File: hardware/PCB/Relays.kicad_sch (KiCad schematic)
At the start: 22 parts, among them K601 SANYOU_SRD_Form_C, K602 SANYOU_SRD_Form_C, K603 SANYOU_SRD_Form_C, Q601 NPN, Q602 NPN, Q603 NPN, U601 PC817C, U602 PC817C, U603 PC817C

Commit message: Rough Layout pcb
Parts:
- removed Q602, Q603: NPN, Package_TO_SOT_SMD:SOT-23, symbol Simulation_SPICE:NPN
- added Q502, Q503: NPN, Package_TO_SOT_SMD:SOT-23, symbol Simulation_SPICE:NPN
- added TP501, TP502, TP503: TestPoint, TestPoint:TestPoint_Pad_D1.5mm, symbol Connector:TestPoint
- J504: renamed from JK_in601; value Relays -> Relays_in; now left out of the parts list
- K501: renamed from K601; now in the parts list
- K502: renamed from K602; now in the parts list
- K503: renamed from K603; now in the parts list
- R501: renamed from R601; JLCPCB Part (none) -> C17557
- R502: renamed from R602; JLCPCB Part (none) -> C17557
- R503: renamed from R603; JLCPCB Part (none) -> C17557
- R504: renamed from R604; JLCPCB Part (none) -> C17557
- R505: renamed from R605; JLCPCB Part (none) -> C17557
- R506: renamed from R606; JLCPCB Part (none) -> C17557
- U501: renamed from U601; Link (none) -> https://pl.aliexpress.com/item/1005009030409853.html?spm=a2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
- U502: renamed from U602; Link (none) -> https://pl.aliexpress.com/item/1005009030409853.html?spm=a2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
- U503: renamed from U603; Link (none) -> https://pl.aliexpress.com/item/1005009030409853.html?spm=a2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
- renumbered D601 to D501, D602 to D502, D603 to D503, JK_out601 to J501, JK_out602 to J502, JK_out603 to J503, Q601 to Q501
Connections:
- net GND: now also Q502.3 (E), Q503.3 (E)
- net K1_opto_out: now also TP501.1
- net K2_QC_K: now also Q502.1 (C)
- net K2_Q_B: now also Q502.2 (B)
- net K2_opto_out: now also TP502.1
- net K3_QC_K: now also Q503.1 (C)
- net K3_Q_B: now also Q503.2 (B)
- net K3_opto_out: now also TP503.1
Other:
- moved on the sheet: J504

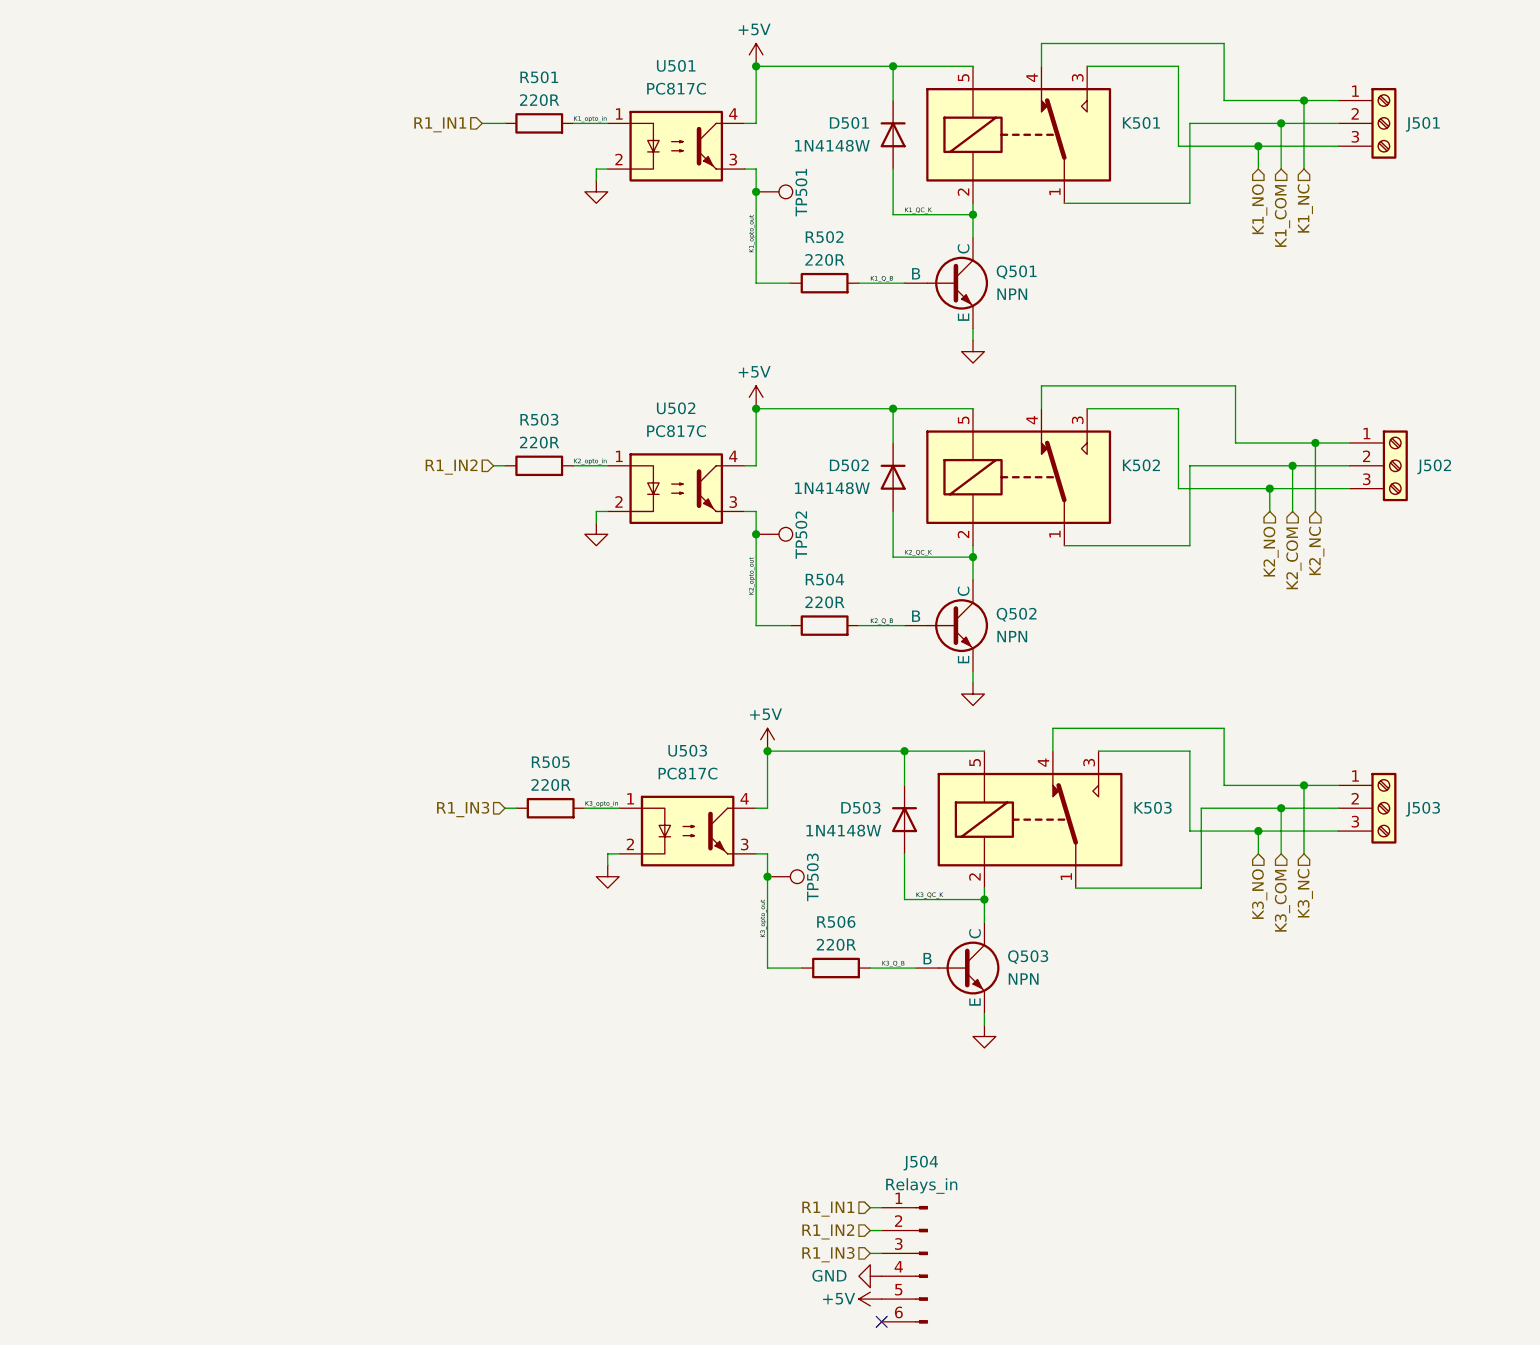
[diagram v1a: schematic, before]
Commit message: XL4015 CC, relays
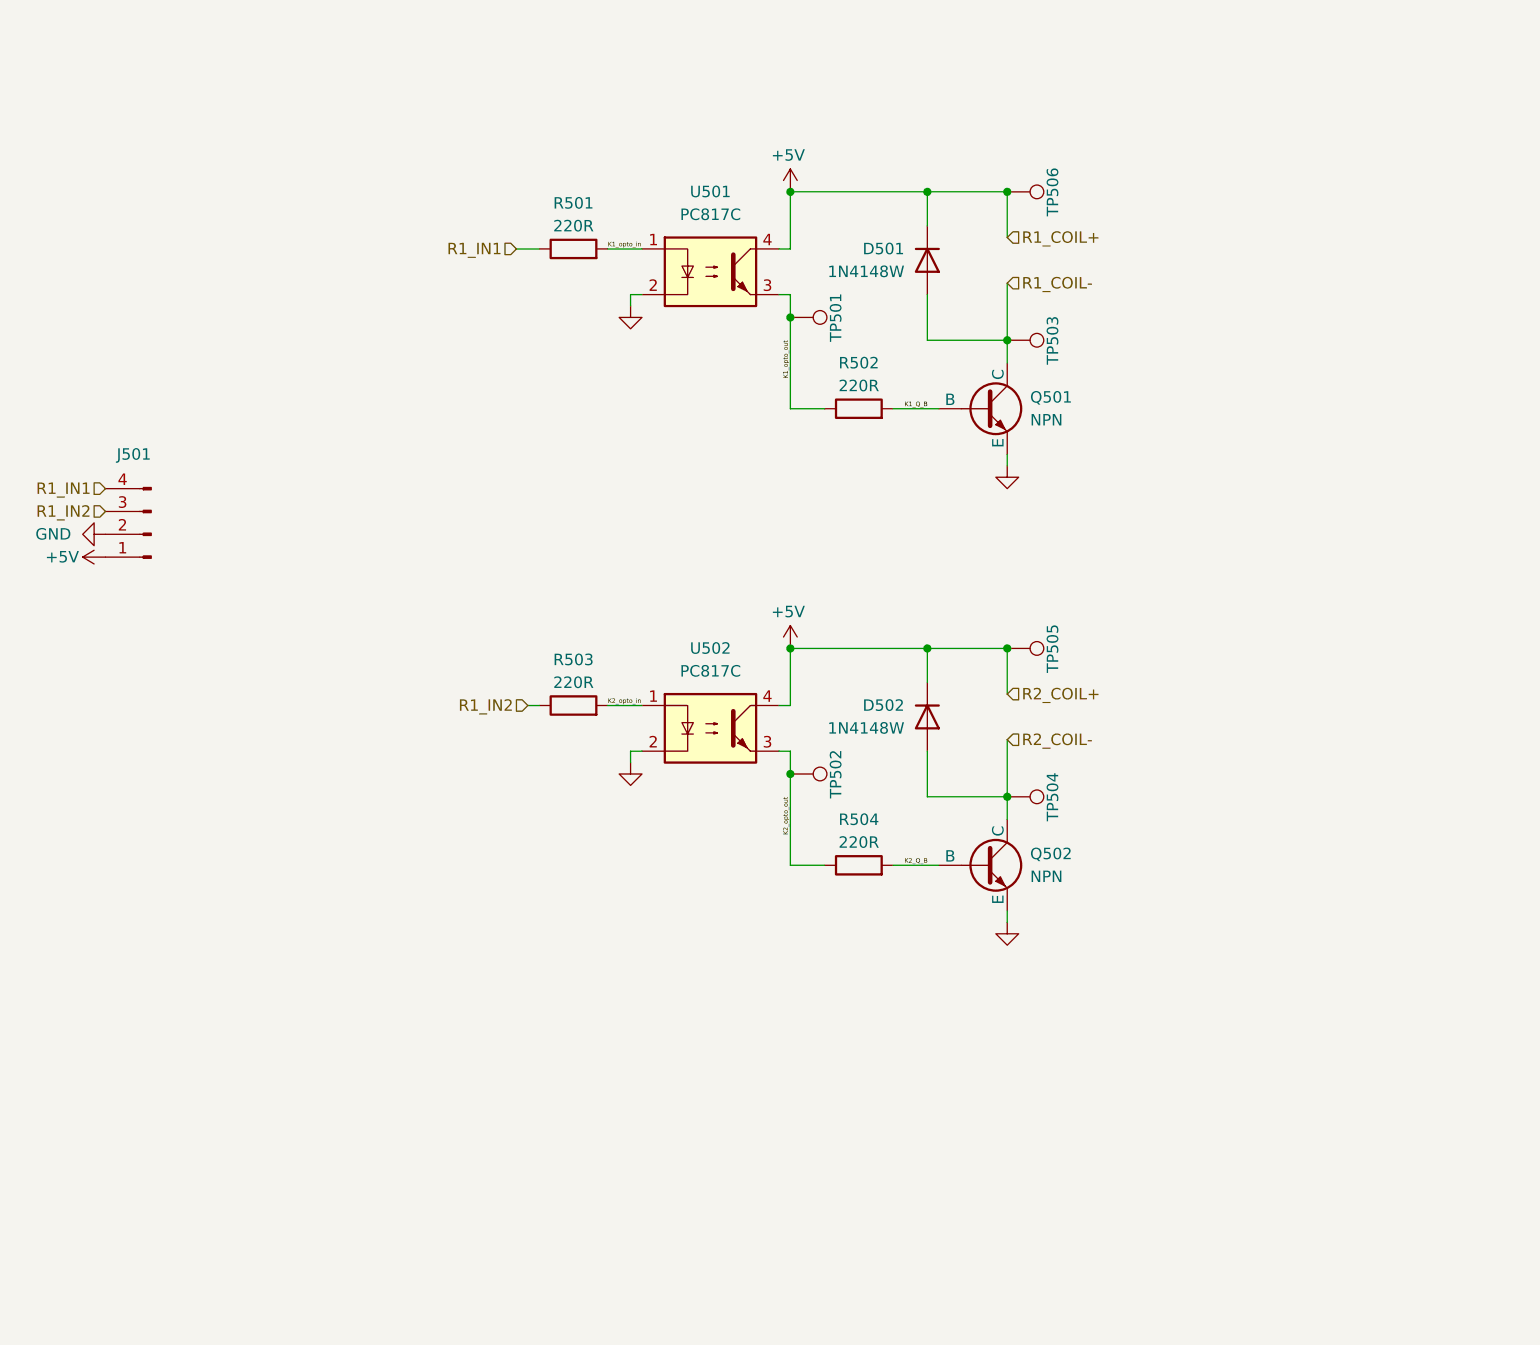
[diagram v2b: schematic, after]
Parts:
- removed D503: 1N4148W, Diode_SMD:D_SOD-123, symbol Device:D
- removed J501, J502, J503: Screw_Terminal_01x03, TerminalBlock_Phoenix:TerminalBlock_Phoenix_MKDS-1,5-3_1x03_P5.00mm_Horizontal, symbol Connector:Screw_Terminal_01x03
- removed J504: Relays_in, Connector_PinHeader_2.54mm:PinHeader_1x06_P2.54mm_Vertical, symbol Connector:Conn_01x06_Pin
- removed K501, K502, K503: SANYOU_SRD_Form_C, Relay_THT:Relay_SPDT_SANYOU_SRD_Series_Form_C, symbol Relay:SANYOU_SRD_Form_C
- removed Q503: NPN, Package_TO_SOT_SMD:SOT-23, symbol Simulation_SPICE:NPN
- removed R505, R506: 220R, Resistor_SMD:R_0805_2012Metric, symbol Device:R
- removed U503: PC817C, Package_DIP:DIP-4_W7.62mm_LongPads, symbol Isolator:VO615A
- added J501: Conn_01x04_Pin, symbol Connector:Conn_01x04_Pin
- added TP504, TP505, TP506: TestPoint, TestPoint:TestPoint_Pad_D1.5mm, symbol Connector:TestPoint
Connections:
- net K3_opto_out is gone; now on net R1_COIL-: TP503.1
- net +5V: now also J501.1 (Pin_1), TP505.1, TP506.1
- net GND: now also J501.2 (Pin_2)
- net R1_IN1: now also J501.4 (Pin_4)
- net R1_IN2: now also J501.3 (Pin_3)
- net K1_QC_K renamed R1_COIL-
- net K2_QC_K renamed R2_COIL-
- net R2_COIL-: now also TP504.1
- no-connect marks 1 -> 0
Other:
- moved on the sheet: D501, D502, Q501, Q502, R501, R502, R503, R504, TP501, TP502, U501, U502

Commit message: pcb
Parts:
- J501: footprint (none) -> Connector_PinHeader_2.54mm:PinHeader_1x04_P2.54mm_Vertical; now not fitted; now left out of the parts list
- TP501: renamed from TP506; footprint TestPoint:TestPoint_Pad_D1.5mm -> TestPoint:TestPoint_THTPad_D1.5mm_Drill0.7mm
- TP502: renamed from TP501; footprint TestPoint:TestPoint_Pad_D1.5mm -> TestPoint:TestPoint_THTPad_D1.5mm_Drill0.7mm
- TP503: footprint TestPoint:TestPoint_Pad_D1.5mm -> TestPoint:TestPoint_THTPad_D1.5mm_Drill0.7mm
- TP504: renamed from TP505; footprint TestPoint:TestPoint_Pad_D1.5mm -> TestPoint:TestPoint_THTPad_D1.5mm_Drill0.7mm
- TP505: renamed from TP502; footprint TestPoint:TestPoint_Pad_D1.5mm -> TestPoint:TestPoint_THTPad_D1.5mm_Drill0.7mm
- TP506: renamed from TP504; footprint TestPoint:TestPoint_Pad_D1.5mm -> TestPoint:TestPoint_THTPad_D1.5mm_Drill0.7mm

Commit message: PCB final routing
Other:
- company: (none) -> Authors: D. Ledzianowski K. Lewandowska T. Majchrzak
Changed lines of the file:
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@@
 	(generator_version "9.0")
 	(paper "A4")
+	(title_block
+		(date "2025-12-07")
+		(rev "1.0")
+		(company "Authors: D. Ledzianowski K. Lewandowska T. Majchrzak")
+	)
 	(junction
 		(at 165.1 111.76)

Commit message: PCB final design
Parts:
- D501, D502: JLCPCB Part C81598 -> C81598; MFR Part 1N4148W -> 1N4148W
- J501: now in the parts list
- Q501, Q502: JLCPCB Part C20526 -> C20526; MFR Part MMBT3904(RANGE:100-300) -> MMBT3904(RANGE:100-300)
- R501, R502, R503, R504: Manufacturer UNI-ROYAL(Uniroyal Elec) -> UNI-ROYAL(Uniroyal Elec)
- U501, U502: value PC817C -> LTV-217; footprint Package_DIP:DIP-4_W7.62mm_LongPads -> Package_SO:SOP-4_4.4x2.6mm_P1.27mm; JLCPCB Part (none) -> C115450; Link https://pl.aliexpress.com/item/1005009030409853.html?spm=a2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 -> https://jlcpcb.com/partdetail/LiteOn-LTV_217_BG/C115450; MFR Part (none) -> LTV-217-B-G; Manufacturer (none) -> Lite-On
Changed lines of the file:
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@@
 			)
 		)
-		(property "Manufacturer" "UNI-ROYAL(Uniroyal Elec) "
+		(property "Manufacturer" "UNI-ROYAL(Uniroyal Elec)"
 			(at 148.59 135.89 90)
 			(effects
@@
 			)
 		)
-		(property "Manufacturer" "UNI-ROYAL(Uniroyal Elec) "
+		(property "Manufacturer" "UNI-ROYAL(Uniroyal Elec)"
 			(at 116.84 118.11 90)
 			(effects
@@
 			)
 		)
-		(property "JLCPCB Part" " C20526"
+		(property "JLCPCB Part" "C20526"
 			(at 162.56 135.89 0)
 			(effects
@@
 			)
 		)
-		(property "MFR Part" " MMBT3904(RANGE:100-300)"
+		(property "MFR Part" "MMBT3904(RANGE:100-300)"
 			(at 162.56 135.89 0)
 			(effects
@@
 			)
 		)
-		(property "JLCPCB Part" " C81598"
+		(property "JLCPCB Part" "C81598"
 			(at 156.21 68.58 90)
 			(effects
@@
 			)
 		)
-		(property "MFR Part" " 1N4148W"
+		(property "MFR Part" "1N4148W"
 			(at 156.21 68.58 90)
 			(effects
@@
 		(unit 1)
 		(exclude_from_sim no)
-		(in_bom no)
+		(in_bom yes)
 		(on_board yes)
 		(dnp yes)
@@
 			)
 		)
-		(property "Value" "PC817C"
+		(property "Value" "LTV-217"
 			(at 132.08 63.5 0)
 			(effects
@@
 			)
 		)
-		(property "Footprint" "Package_DIP:DIP-4_W7.62mm_LongPads"
+		(property "Footprint" "Package_SO:SOP-4_4.4x2.6mm_P1.27mm"
 			(at 132.08 69.85 0)
 			(effects
@@
 			)
 		)
-		(property "Link" "https://pl.aliexpress.com/item/1005009030409853.html?spm=a2g0o.order_list.order_list_main.10.1b421c24vYZudn&gatewayAdapt=glo2pol"
+		(property "Link" "https://jlcpcb.com/partdetail/LiteOn-LTV_217_BG/C115450"
 			(at 132.08 69.85 0)
 			(effects
@@
 		)
 		(property "Sim.Type" ""
+			(at 132.08 69.85 0)
+			(effects
+				(font
+					(size 1.27 1.27)
+				)
+				(hide yes)
+			)
+		)
+		(property "JLCPCB Part" "C115450"
+			(at 132.08 69.85 0)
+			(effects
+				(font
+					(size 1.27 1.27)
+				)
+				(hide yes)
+			)
+		)
+		(property "MFR Part" "LTV-217-B-G"
+			(at 132.08 69.85 0)
+			(effects
+				(font
+					(size 1.27 1.27)
+				)
+				(hide yes)
+			)
+		)
+		(property "Manufacturer" "Lite-On"
 			(at 132.08 69.85 0)
 			(effects
@@
 			)
 		)
-		(property "JLCPCB Part" " C20526"
+		(property "JLCPCB Part" "C20526"
 			(at 162.56 85.09 0)
 			(effects
@@
 			)
 		)
-		(property "MFR Part" " MMBT3904(RANGE:100-300)"
+		(property "MFR Part" "MMBT3904(RANGE:100-300)"
 			(at 162.56 85.09 0)
 			(effects
@@
 			)
 		)
-		(property "Manufacturer" "UNI-ROYAL(Uniroyal Elec) "
+		(property "Manufacturer" "UNI-ROYAL(Uniroyal Elec)"
 			(at 148.59 85.09 90)
 			(effects
@@
 			)
 		)
-		(property "Manufacturer" "UNI-ROYAL(Uniroyal Elec) "
+		(property "Manufacturer" "UNI-ROYAL(Uniroyal Elec)"
 			(at 116.84 67.31 90)
 			(effects
@@
 			)
 		)
-		(property "Value" "PC817C"
+		(property "Value" "LTV-217"
 			(at 132.08 114.3 0)
 			(effects
@@
 			)
 		)
-		(property "Footprint" "Package_DIP:DIP-4_W7.62mm_LongPads"
+		(property "Footprint" "Package_SO:SOP-4_4.4x2.6mm_P1.27mm"
 			(at 132.08 120.65 0)
 			(effects
@@
 			)
 		)
-		(property "Link" "https://pl.aliexpress.com/item/1005009030409853.html?spm=a2g0o.order_list.order_list_main.10.1b421c24vYZudn&gatewayAdapt=glo2pol"
+		(property "Link" "https://jlcpcb.com/partdetail/LiteOn-LTV_217_BG/C115450"
 			(at 132.08 120.65 0)
 			(effects
@@
 		)
 		(property "Sim.Type" ""
+			(at 132.08 120.65 0)
+			(effects
+				(font
+					(size 1.27 1.27)
+				)
+				(hide yes)
+			)
+		)
+		(property "JLCPCB Part" "C115450"
+			(at 132.08 120.65 0)
+			(effects
+				(font
+					(size 1.27 1.27)
+				)
+				(hide yes)
+			)
+		)
+		(property "MFR Part" "LTV-217-B-G"
+			(at 132.08 120.65 0)
+			(effects
+				(font
+					(size 1.27 1.27)
+				)
+				(hide yes)
+			)
+		)
+		(property "Manufacturer" "Lite-On"
 			(at 132.08 120.65 0)
 			(effects
@@
 			)
 		)
-		(property "JLCPCB Part" " C81598"
+		(property "JLCPCB Part" "C81598"
 			(at 156.21 119.38 90)
 			(effects
@@
 			)
 		)
-		(property "MFR Part" " 1N4148W"
+		(property "MFR Part" "1N4148W"
 			(at 156.21 119.38 90)
 			(effects

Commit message: usb, sd
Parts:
- J501: now fitted
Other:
- title: (none) -> Stanowisko do badania parametrów pracy ogniw Li-Ion Li-Pol
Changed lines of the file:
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@@
 	(paper "A4")
 	(title_block
-		(date "2025-12-07")
-		(rev "1.0")
+		(title "Stanowisko do badania parametrów pracy ogniw Li-Ion Li-Pol")
+		(date "2025-12-10")
+		(rev "0.1")
 		(company "Authors: D. Ledzianowski K. Lewandowska T. Majchrzak")
 	)
@@
 		(in_bom yes)
 		(on_board yes)
-		(dnp yes)
+		(dnp no)
 		(property "Reference" "J501"
 			(at 69.85 90.17 0)
